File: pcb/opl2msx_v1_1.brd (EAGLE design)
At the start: 102.7 x 64.3 mm, 26 parts, among them IC1 74HC32N, IC2 74HC138N, IC3 YM3812, IC4 Y3014B, IC5 LM358N, IC6 7404N, IC7 LM386N-1, IC8 29EE010N, J1 AUDIO_JACK_3.5MM_KIT

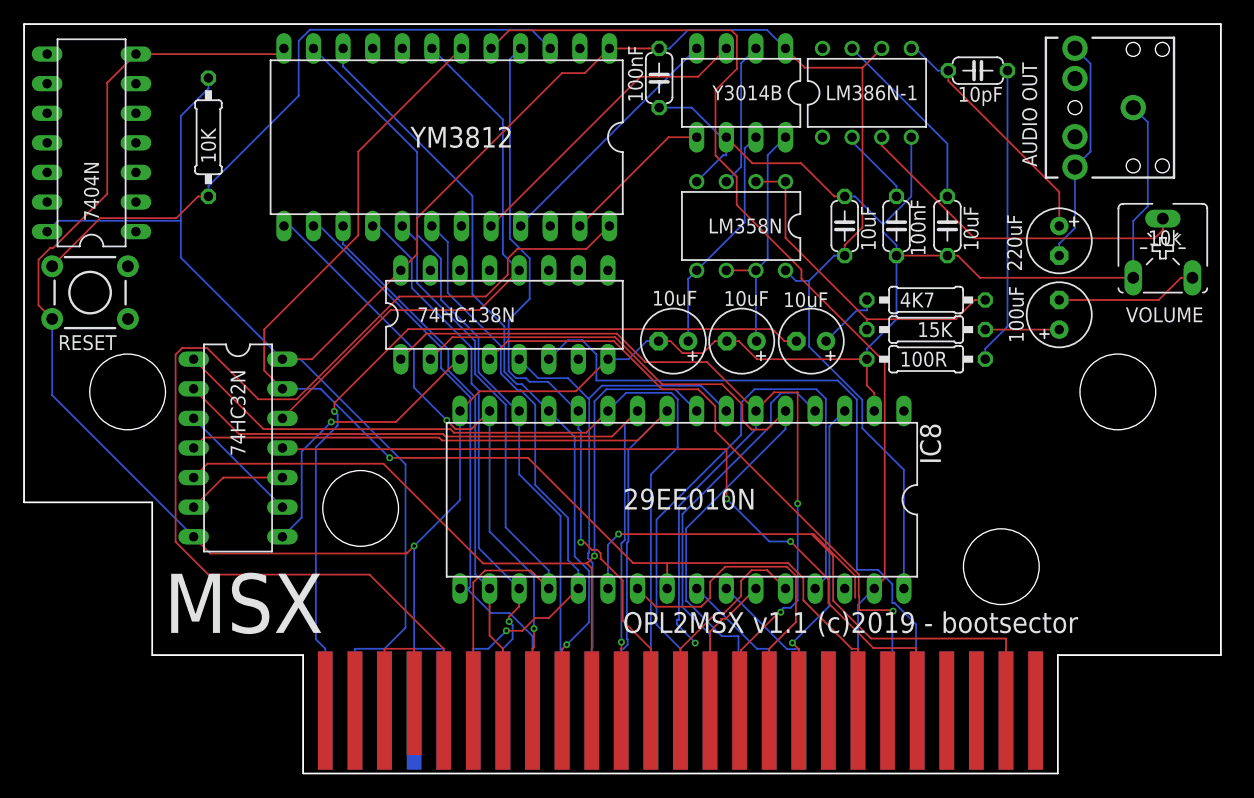
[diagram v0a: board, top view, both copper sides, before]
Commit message: Fixed PCB version 1.1. Removed unused 7404 IC
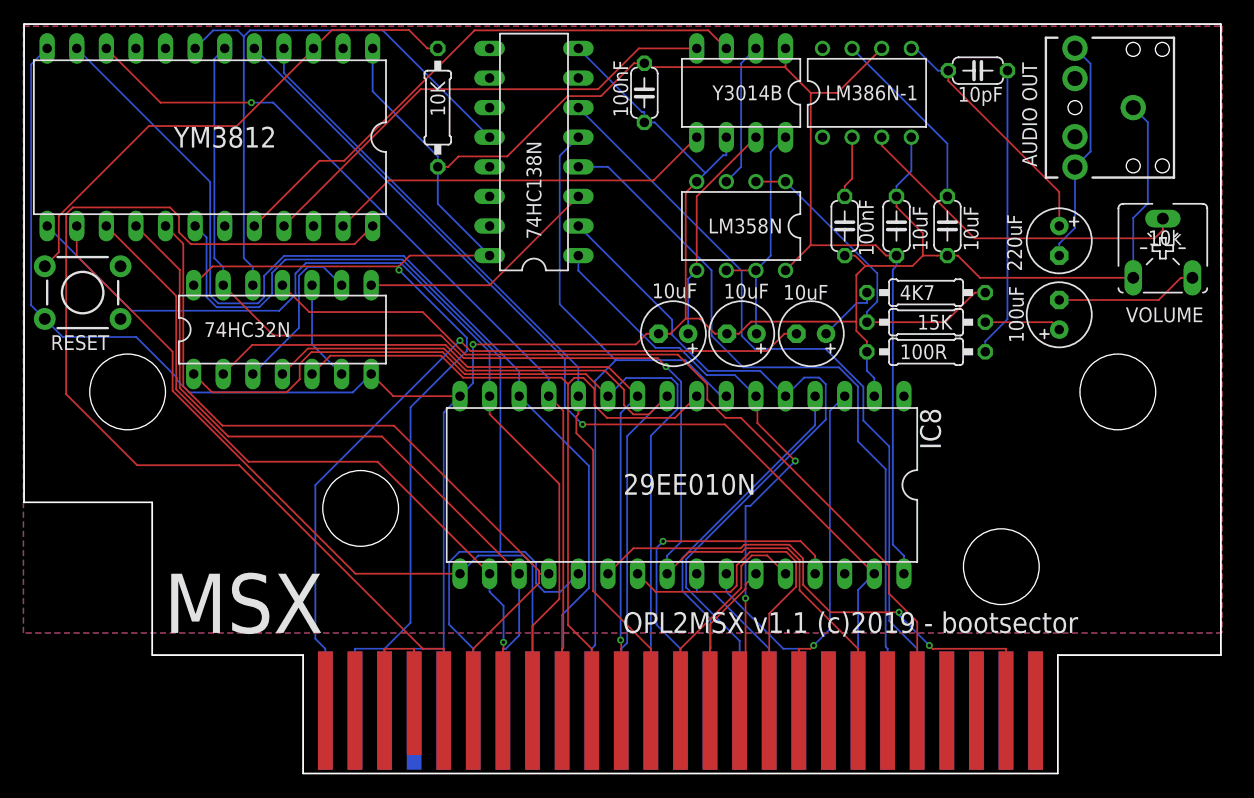
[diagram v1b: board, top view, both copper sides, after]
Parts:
- removed IC6: 7404N, 74xx-us:DIL14
- moved IC3 20.3 mm to (16.0, 54.6)
- moved R7 19.8 mm to (35.6, 57.1), turned to 270 degrees
- moved IC2 14.2 mm to (43.8, 53.3), turned to 90 degrees
- moved IC1 10.9 mm to (22.2, 38.1), turned to 0 degrees
- moved C5 4.45 mm to (70.5, 47.0)
- moved C8 4.45 mm to (74.9, 47.0)
- moved C1 1.80 mm to (53.3, 58.4)
- moved IC8 1.27 mm to (56.5, 24.8)
- moved S1 0.63 mm to (5.08, 41.3)
- moved C10 0.63 mm to (67.6, 37.7)
- moved C2 0.63 mm to (61.6, 37.7)
- moved C3 0.63 mm to (55.8, 37.7)
- moved R2 0.63 mm to (77.5, 38.7)
- moved R3 0.63 mm to (77.5, 41.3)
- moved R5 0.63 mm to (77.5, 36.2)
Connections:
- net +5V: no longer IC6.14
- net GND: no longer IC6.7
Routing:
- net A6: track 95.5 -> 51.6 mm, vias 3 -> 2
- net D7: track 53.0 -> 83.2 mm, vias 1 -> 0
- net D2: track 54.8 -> 81.1 mm, vias 2 -> 0
- net D1: track 65.8 -> 92.2 mm
- net A14: track 55.0 -> 30.7 mm, vias 0 -> 1
- net N$13: track 26.5 -> 48.1 mm
- net N$15: track 13.2 -> 33.5 mm
- net N$14: track 21.5 -> 41.7 mm
- net D3: track 51.5 -> 68.4 mm
- net A5: track 47.5 -> 63.5 mm
- net D5: track 47.9 -> 63.6 mm, vias 1 -> 0
- net D4: track 47.3 -> 62.2 mm, vias 0 -> 1
- net D0: track 66.8 -> 78.8 mm
- net SLTSL: track 57.6 -> 45.7 mm, vias 1 -> 2
- net D6: track 54.9 -> 66.7 mm
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- added copper zone on layer 1, net GND
- added copper zone on layer 16, net GND

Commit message: Updated PCB v1.1 layout
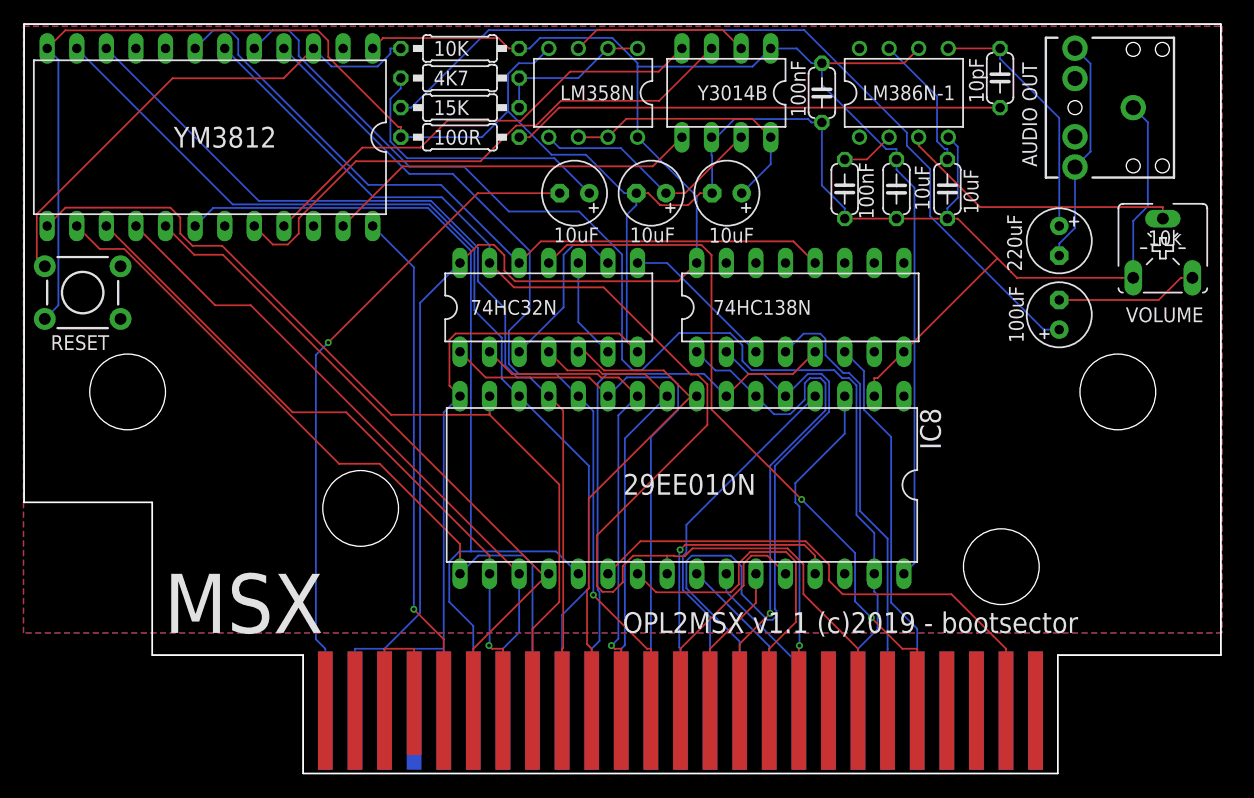
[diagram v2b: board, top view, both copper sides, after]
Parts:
- moved R2 44.0 mm to (37.5, 57.1), turned to 0 degrees
- moved R3 44.0 mm to (37.5, 59.7)
- moved R5 44.0 mm to (37.5, 54.6)
- moved IC2 26.5 mm to (66.7, 40.0), turned to 0 degrees
- moved C10 23.6 mm to (47.3, 49.8)
- moved IC1 22.9 mm to (45.1, 40.0)
- moved IC5 17.1 mm to (48.9, 58.4)
- moved C1 15.2 mm to (68.5, 58.4)
- moved C3 12.2 mm to (53.9, 49.8)
- moved C2 12.1 mm to (60.4, 49.8)
- moved R7 5.43 mm to (37.5, 62.2), turned to 0 degrees
- moved C5 3.17 mm to (70.5, 50.2)
- moved C6 3.17 mm to (79.3, 50.2)
- moved C8 3.17 mm to (74.9, 50.2), turned to 270 degrees
- moved IC7 3.17 mm to (75.6, 58.4)
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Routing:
- net N$1: track 6.61 -> 72.9 mm
- net CLK: track 91.5 -> 44.1 mm, vias 0 -> 1
- net M1: track 67.4 -> 33.4 mm
- net A3: track 66.3 -> 40.4 mm
- net A1: track 75.8 -> 50.2 mm
- net IORQ: track 64.0 -> 38.7 mm
- net A4: track 66.8 -> 42.6 mm
- net GND: track 237.9 -> 262.1 mm, vias 1 -> 0
- net A2: track 66.0 -> 42.9 mm
- net N$7: track 5.49 -> 24.7 mm
- net N$12: track 24.9 -> 42.3 mm
- net WR: track 86.6 -> 103.8 mm, vias 1 -> 0
- net AUDIO: track 29.4 -> 13.8 mm
- net BUSDIR: track 76.2 -> 62.1 mm, vias 0 -> 2
- net A5: track 63.5 -> 49.8 mm
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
